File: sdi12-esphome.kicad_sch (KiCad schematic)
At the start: 12 parts, among them J1 Screw_Terminal_01x03, Q1 2N7002, U1 ESP32_NODEMCU, U2 74LVC1G125

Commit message: Schematic: Add 12V boost converter for sensor power
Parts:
- added C3, C4: 10µF, Capacitor_SMD:C_0805_2012Metric_Pad1.18x1.45mm_HandSolder, symbol Device:C
- added D2: MBR0540, Diode_SMD:D_SOD-123, symbol Diode:MBR0540
- added L1: 4.7µH, Inductor_SMD:L_1008_2520Metric_Pad1.43x2.20mm_HandSolder, symbol Device:L
- added R6: 1M±1%, Resistor_SMD:R_0805_2012Metric_Pad1.20x1.40mm_HandSolder, symbol Device:R
- added R7: 56k±1%, symbol Device:R
- added R8: 120k±1%, symbol Device:R
- added U3: MCP1661, Package_TO_SOT_SMD:SOT-23-5, symbol Driver_LED:MCP1662-xOT
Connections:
- net +5V: now also C3.1, L1.1, U3.5 (V_{IN})
- net GND: now also GD1.1, C3.2, C4.2, R8.2, U3.2 (GND)
- net at GD1.3: now also R2.2
- net VCC Enable: now reaches U1.J5_13 (G32)
- net VCC Enable: now also U3.4 (EN)
- new net: D2.2 (A), L1.2, U3.1 (SW)
- new net: R6.2, U3.3 (V_{FB})
- new net: R6.1, R7.2
- new net +12V: C4.1, D2.1 (K), R7.1, R8.1
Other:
- note added: "Boost Conversion 5V->12V"

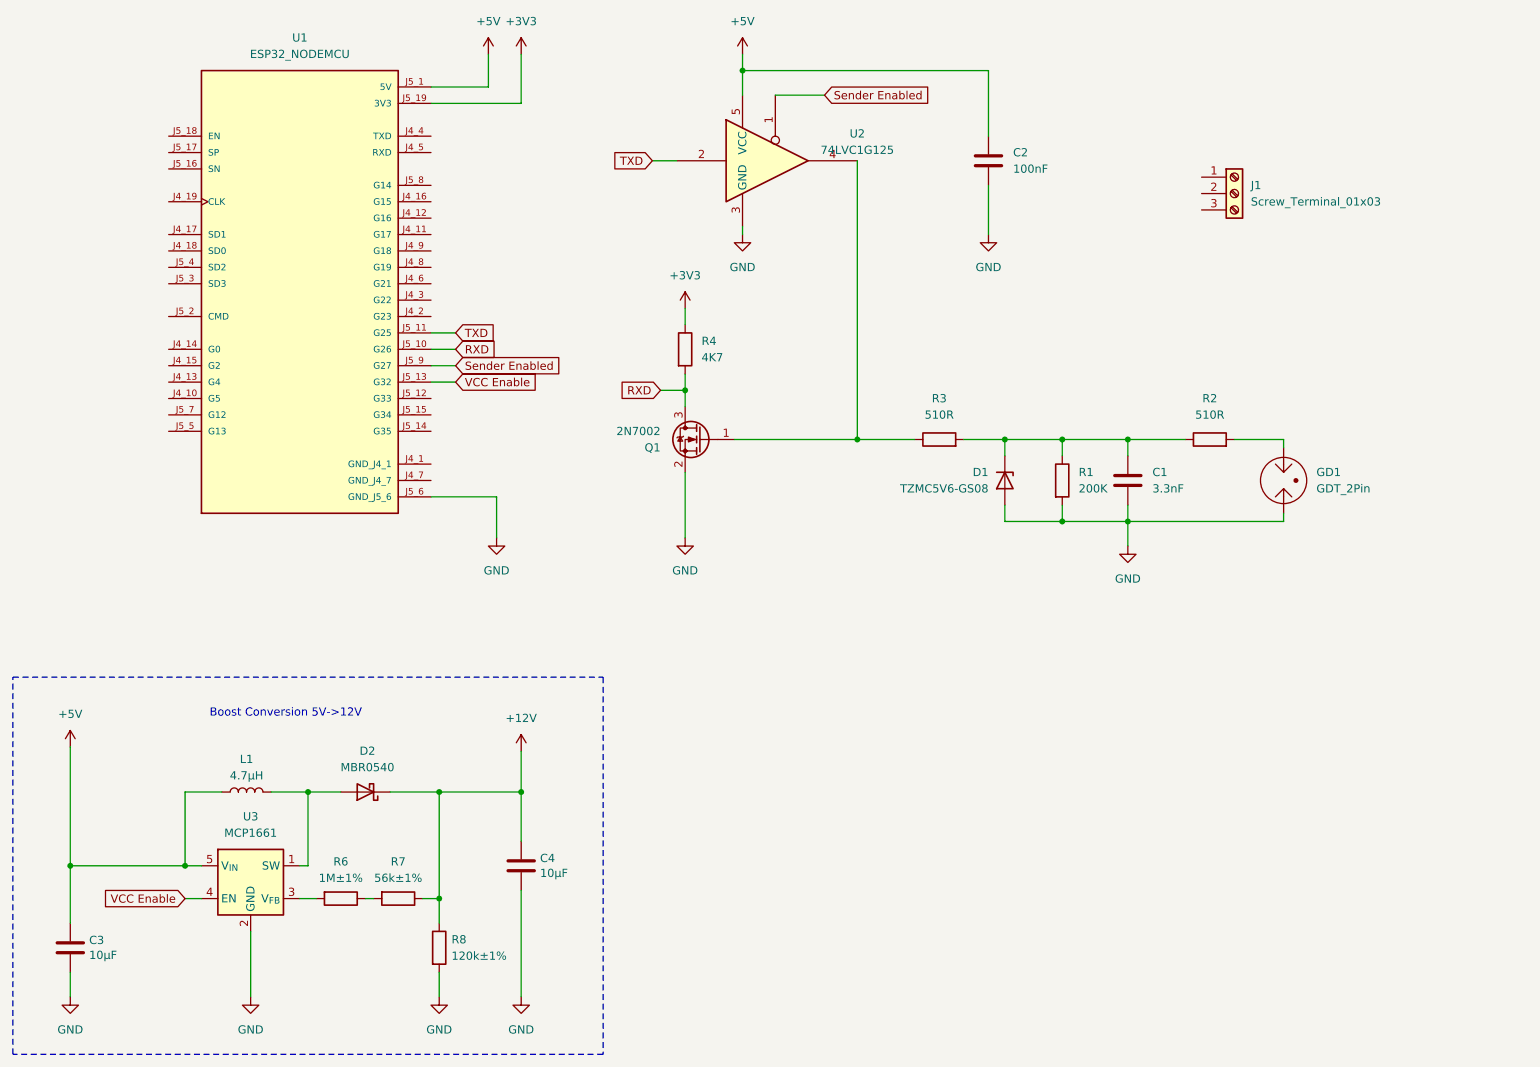
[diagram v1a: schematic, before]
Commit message: schematic: Add BUS terminals, fixup global labels
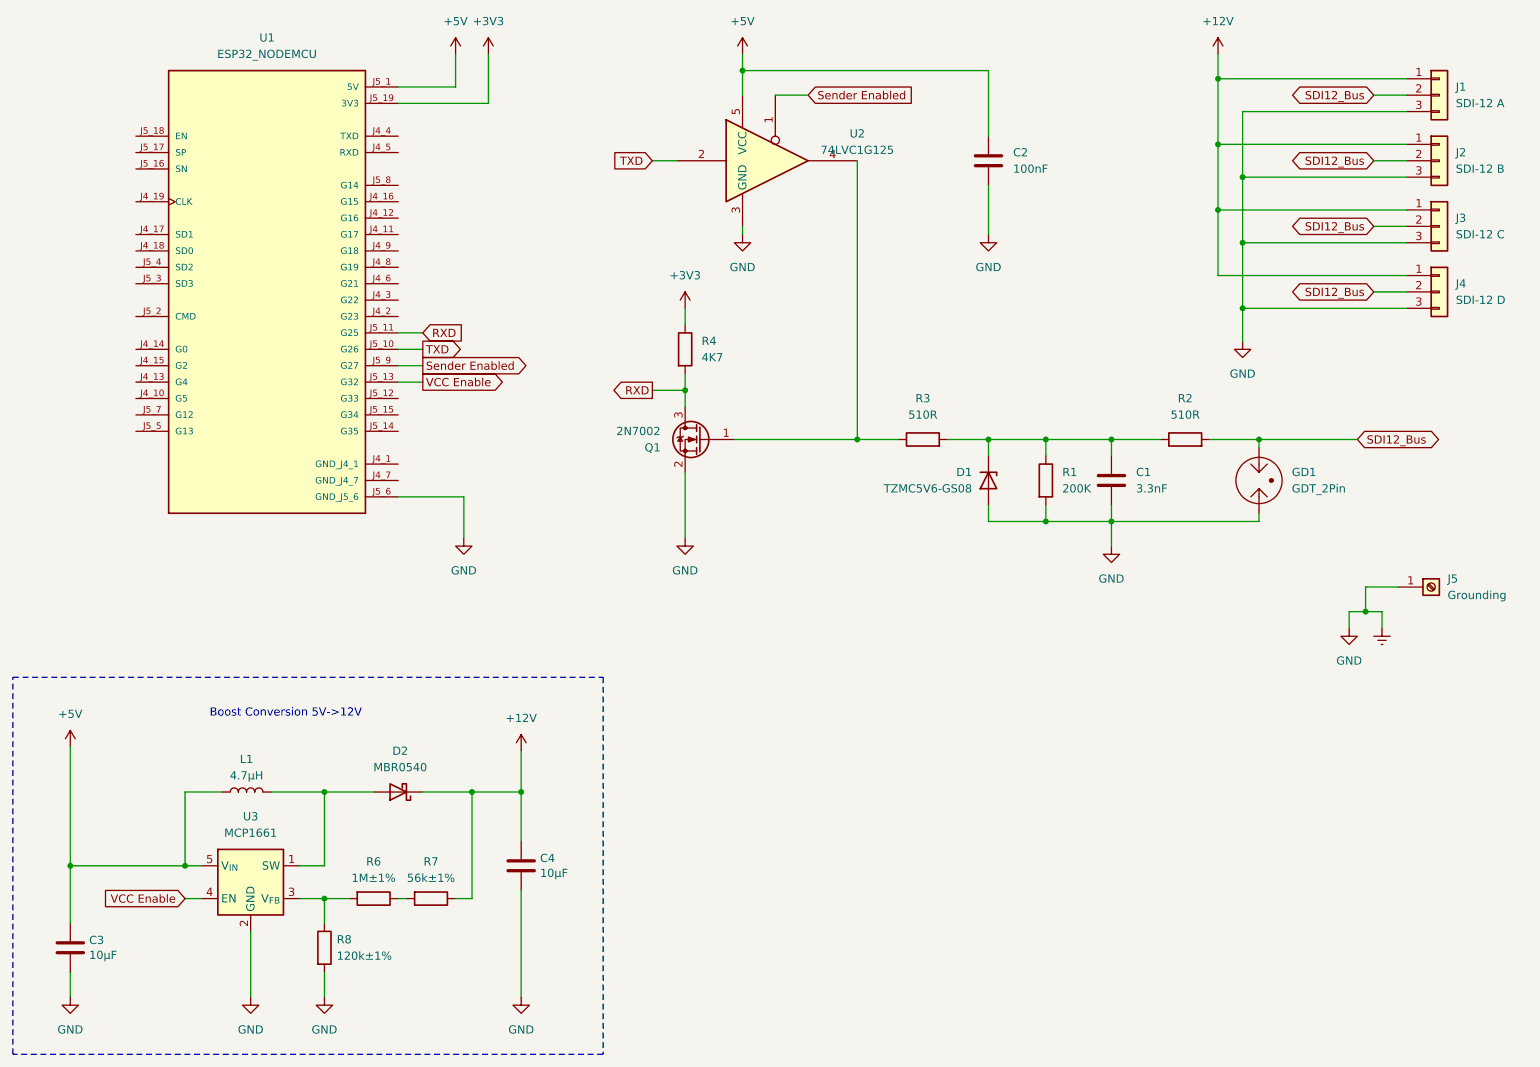
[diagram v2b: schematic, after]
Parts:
- removed J1: Screw_Terminal_01x03, symbol Connector:Screw_Terminal_01x03
- added J1: SDI-12 A, Fraxinas-kicad:Phoenix Contact SPTA 1 3 3,5 1752227, symbol Connector_Generic:Conn_01x03
- added J2: SDI-12 B, Fraxinas-kicad:Phoenix Contact SPTA 1 3 3,5 1752227, symbol Connector_Generic:Conn_01x03
- added J3: SDI-12 C, Fraxinas-kicad:Phoenix Contact SPTA 1 3 3,5 1752227, symbol Connector_Generic:Conn_01x03
- added J4: SDI-12 D, Fraxinas-kicad:Phoenix Contact SPTA 1 3 3,5 1752227, symbol Connector_Generic:Conn_01x03
- added J5: Grounding, MountingHole:MountingHole_4.3mm_M4_ISO7380_Pad_TopBottom, symbol Connector:Screw_Terminal_01x01
- GD1: footprint (none) -> Diode_THT:D_P600_R-6_P12.70mm_Horizontal
- R7, R8: footprint (none) -> Resistor_SMD:R_0805_2012Metric_Pad1.20x1.40mm_HandSolder
- U1: footprint ESP32_NODEMCU:MODULE_ESP32_NODEMCU -> Fraxinas-kicad:MODULE_ESP32_NODEMCU
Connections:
- net +12V: now also J1.1 (Pin_1), J2.1 (Pin_1), J3.1 (Pin_1), J4.1 (Pin_1); no longer R8.1
- net RXD: now also U1.J5_11 (G25); no longer U1.J5_10 (G26)
- net TXD: now also U1.J5_10 (G26); no longer U1.J5_11 (G25)
- net at R6.2, U3.3 (V_{FB}): now also R8.1
- net SDI12_Bus: now reaches GD1.3, R2.2
- net SDI12_Bus: now also J1.2 (Pin_2), J2.2 (Pin_2), J3.2 (Pin_2), J4.2 (Pin_2)
- net GND renamed Earth
- net Earth: now also J1.3 (Pin_3), J2.3 (Pin_3), J3.3 (Pin_3), J4.3 (Pin_3), J5.1 (Pin_1)
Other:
- moved on the sheet: C1, D1, D2, GD1, R1, R2, R3, R6, R7, R8, U1

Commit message: schematic: Fix GND Net name, import project settings (trace widths etc.)
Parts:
- U3: footprint Package_TO_SOT_SMD:SOT-23-5 -> Package_TO_SOT_SMD:SOT-23-5_HandSoldering
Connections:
- net Earth is gone; now on net GND: C1.2, C2.2, C3.2, C4.2, D1.2 (A), GD1.1, J1.3 (Pin_3), J2.3 (Pin_3), J3.3 (Pin_3), J4.3 (Pin_3), J5.1 (Pin_1), Q1.2 (S), R1.2, R8.2, U1.J5_6 (GND_J5_6), U2.3 (GND), U3.2 (GND)
- net GND: now reaches U1.J4_1 (GND_J4_1)
- net GND: now also U1.J4_7 (GND_J4_7)
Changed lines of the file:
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@@
   (junction (at 186.69 97.79) (diameter 0) (color 0 0 0 0)
   )
+  (junction (at 86.36 104.14) (diameter 0) (color 0 0 0 0)
+  )
+  (junction (at 86.36 106.68) (diameter 0) (color 0 0 0 0)
+  )
   (junction (at 105.41 152.4) (diameter 0) (color 0 0 0 0)
   )
@@
   (junction (at 213.36 52.07) (diameter 0) (color 0 0 0 0)
   )
-  (junction (at 236.22 124.46) (diameter 0) (color 0 0 0 0)
-  )
   (junction (at 97.79 152.4) (diameter 0) (color 0 0 0 0)
   )
@@
     (stroke (width 0) (type default))
   )
-  (wire (pts (xy 233.68 124.46) (xy 233.68 127))
-    (stroke (width 0) (type default))
-  )
   (wire (pts (xy 86.36 86.36) (xy 90.17 86.36))
     (stroke (width 0) (type default))
@@
     (stroke (width 0) (type default))
   )
-  (wire (pts (xy 236.22 120.65) (xy 236.22 124.46))
+  (wire (pts (xy 236.22 120.65) (xy 236.22 127))
     (stroke (width 0) (type default))
   )
@@
     (stroke (width 0) (type default))
   )
+  (wire (pts (xy 86.36 101.6) (xy 86.36 104.14))
+    (stroke (width 0) (type default))
+  )
   (wire (pts (xy 171.45 97.79) (xy 177.8 97.79))
     (stroke (width 0) (type default))
@@
     (stroke (width 0) (type default))
   )
-  (wire (pts (xy 238.76 124.46) (xy 238.76 127))
-    (stroke (width 0) (type default))
-  )
   (wire (pts (xy 241.3 120.65) (xy 236.22 120.65))
     (stroke (width 0) (type default))
@@
     (stroke (width 0) (type default))
   )
-  (wire (pts (xy 233.68 124.46) (xy 236.22 124.46))
-    (stroke (width 0) (type default))
-  )
   (wire (pts (xy 95.25 168.91) (xy 97.79 168.91))
     (stroke (width 0) (type default))
@@
     (stroke (width 0) (type default))
   )
+  (wire (pts (xy 86.36 104.14) (xy 86.36 106.68))
+    (stroke (width 0) (type default))
+  )
   (wire (pts (xy 53.34 168.91) (xy 55.88 168.91))
     (stroke (width 0) (type default))
@@
   )
   (wire (pts (xy 74.93 168.91) (xy 74.93 172.72))
-    (stroke (width 0) (type default))
-  )
-  (wire (pts (xy 236.22 124.46) (xy 238.76 124.46))
     (stroke (width 0) (type default))
   )
@@
       (effects (font (size 1.27 1.27)))
     )
-    (property "Footprint" "Package_TO_SOT_SMD:SOT-23-5" (at 63.5 184.15 0)
+    (property "Footprint" "Package_TO_SOT_SMD:SOT-23-5_HandSoldering" (at 63.5 184.15 0)
       (effects (font (size 1.27 1.27)) hide)
     )
@@
     )
   )
+  (symbol (lib_id "Diode:BZV55B5V6") (at 196.85 104.14 270) (unit 1)
+    (in_bom yes) (on_board yes) (dnp no) (fields_autoplaced)
+    (property "Reference" "D1" (at 199.39 102.87 90)
+      (effects (font (size 1.27 1.27)) (justify left))
+    )
+    (property "Value" "TZMC5V6-GS08" (at 199.39 105.41 90)
+      (effects (font (size 1.27 1.27)) (justify left))
+    )
+    (property "Footprint" "Diode_SMD:D_MiniMELF" (at 192.405 104.14 0)
+      (effects (font (size 1.27 1.27)) hide)
+    )
+    (property "Datasheet" "https://www.vishay.com/docs/84122/tzm.pdf" (at 196.85 104.14 0)
+      (effects (font (size 1.27 1.27)) hide)
+    )
+    (pin "1")
+    (pin "2")
+    (instances
+      (project "sdi12-esphome"
+        (path "/2cd89c3d-735d-4422-af8b-3a5822a68141"
+          (reference "D1") (unit 1)
+        )
+      )
+    )
+  )
   (symbol (lib_id "power:GND") (at 196.85 114.3 0) (unit 1)
     (in_bom yes) (on_board yes) (dnp no)
@@
         (path "/2cd89c3d-735d-4422-af8b-3a5822a68141"
           (reference "C2") (unit 1)
+        )
+      )
+    )
+  )
+  (symbol (lib_id "Device:C") (at 177.8 104.14 0) (unit 1)
+    (in_bom yes) (on_board yes) (dnp no) (fields_autoplaced)
+    (property "Reference" "C1" (at 173.99 102.87 0)
+      (effects (font (size 1.27 1.27)) (justify right))
+    )
+    (property "Value" "3.3nF" (at 173.99 105.41 0)
+      (effects (font (size 1.27 1.27)) (justify right))
+    )
+    (property "Footprint" "Capacitor_SMD:C_0805_2012Metric_Pad1.18x1.45mm_HandSolder" (at 178.7652 107.95 0)
+      (effects (font (size 1.27 1.27)) hide)
+    )
+    (property "Datasheet" "~" (at 177.8 104.14 0)
+      (effects (font (size 1.27 1.27)) hide)
+    )
+    (pin "1")
+    (pin "2")
+    (instances
+      (project "sdi12-esphome"
+        (path "/2cd89c3d-735d-4422-af8b-3a5822a68141"
+          (reference "C1") (unit 1)
         )
       )
@@
     )
   )
-  (symbol (lib_id "power:GND") (at 233.68 127 0) (unit 1)
+  (symbol (lib_id "power:GND") (at 236.22 127 0) (unit 1)
     (in_bom yes) (on_board yes) (dnp no)
-    (property "Reference" "#PWR019" (at 233.68 133.35 0)
-      (effects (font (size 1.27 1.27)) hide)
-    )
-    (property "Value" "GND" (at 233.68 132.08 0)
-      (effects (font (size 1.27 1.27)))
-    )
-    (property "Footprint" "" (at 233.68 127 0)
-      (effects (font (size 1.27 1.27)) hide)
-    )
-    (property "Datasheet" "" (at 233.68 127 0)
+    (property "Reference" "#PWR019" (at 236.22 133.35 0)
+      (effects (font (size 1.27 1.27)) hide)
+    )
+    (property "Value" "GND" (at 236.22 132.08 0)
+      (effects (font (size 1.27 1.27)))
+    )
+    (property "Footprint" "" (at 236.22 127 0)
+      (effects (font (size 1.27 1.27)) hide)
+    )
+    (property "Datasheet" "" (at 236.22 127 0)
       (effects (font (size 1.27 1.27)) hide)
     )
@@
     )
   )
-  (symbol (lib_id "Device:C") (at 196.85 104.14 0) (unit 1)
-    (in_bom yes) (on_board yes) (dnp no) (fields_autoplaced)
-    (property "Reference" "C1" (at 200.66 102.87 0)
-      (effects (font (size 1.27 1.27)) (justify left))
-    )
-    (property "Value" "3.3nF" (at 200.66 105.41 0)
-      (effects (font (size 1.27 1.27)) (justify left))
-    )
-    (property "Footprint" "Capacitor_SMD:C_0805_2012Metric_Pad1.18x1.45mm_HandSolder" (at 197.8152 107.95 0)
-      (effects (font (size 1.27 1.27)) hide)
-    )
-    (property "Datasheet" "~" (at 196.85 104.14 0)
-      (effects (font (size 1.27 1.27)) hide)
-    )
-    (pin "1")
-    (pin "2")
-    (instances
-      (project "sdi12-esphome"
-        (path "/2cd89c3d-735d-4422-af8b-3a5822a68141"
-          (reference "C1") (unit 1)
-        )
-      )
-    )
-  )
   (symbol (lib_id "Device:R") (at 186.69 104.14 0) (unit 1)
     (in_bom yes) (on_board yes) (dnp no) (fields_autoplaced)
@@
     )
   )
-  (symbol (lib_id "Diode:BZV55B5V6") (at 177.8 104.14 270) (unit 1)
-    (in_bom yes) (on_board yes) (dnp no)
-    (property "Reference" "D1" (at 175.26 102.87 90)
-      (effects (font (size 1.27 1.27)) (justify right))
-    )
-    (property "Value" "TZMC5V6-GS08" (at 175.26 105.41 90)
-      (effects (font (size 1.27 1.27)) (justify right))
-    )
-    (property "Footprint" "Diode_SMD:D_MiniMELF" (at 173.355 104.14 0)
-      (effects (font (size 1.27 1.27)) hide)
-    )
-    (property "Datasheet" "https://www.vishay.com/docs/84122/tzm.pdf" (at 177.8 104.14 0)
-      (effects (font (size 1.27 1.27)) hide)
-    )
-    (pin "1")
-    (pin "2")
-    (instances
-      (project "sdi12-esphome"
-        (path "/2cd89c3d-735d-4422-af8b-3a5822a68141"
-          (reference "D1") (unit 1)
-        )
-      )
-    )
-  )
   (symbol (lib_id "power:+12V") (at 105.41 146.05 0) (unit 1)
     (in_bom yes) (on_board yes) (dnp no) (fields_autoplaced)
@@
         )
       )
-    )
-  )
-  (symbol (lib_id "power:Earth") (at 238.76 127 0) (unit 1)
-    (in_bom yes) (on_board yes) (dnp no) (fields_autoplaced)
-    (property "Reference" "#PWR018" (at 238.76 133.35 0)
-      (effects (font (size 1.27 1.27)) hide)
-    )
-    (property "Value" "Earth" (at 238.76 130.81 0)
-      (effects (font (size 1.27 1.27)) hide)
-    )
-    (property "Footprint" "" (at 238.76 127 0)
-      (effects (font (size 1.27 1.27)) hide)
-    )
-    (property "Datasheet" "~" (at 238.76 127 0)
-      (effects (font (size 1.27 1.27)) hide)
-    )
-    (pin "1")
-    (instances
-      (project "sdi12-esphome"
-        (path "/2cd89c3d-735d-4422-af8b-3a5822a68141"
-          (reference "#PWR018") (unit 1)
-        )
-      )
